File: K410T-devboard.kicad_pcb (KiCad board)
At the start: 2 copper layers, 120 x 120 mm, 30 parts, among them U1 XC7K410T-2FFG900I

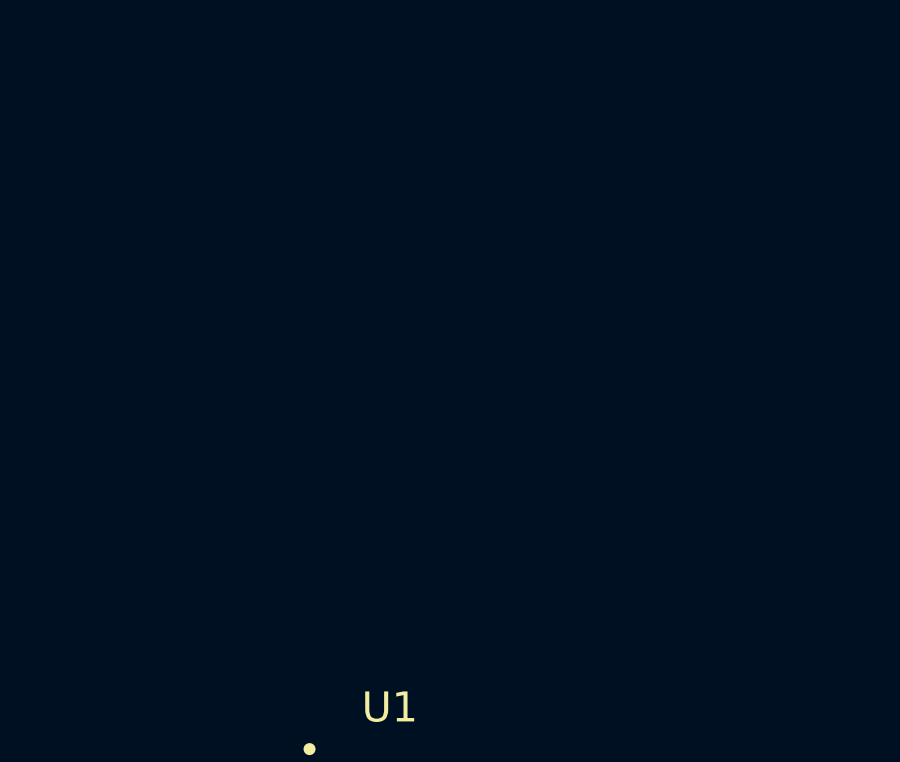
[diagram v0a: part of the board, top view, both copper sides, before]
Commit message: Add MT41K512M8DA DDR3L
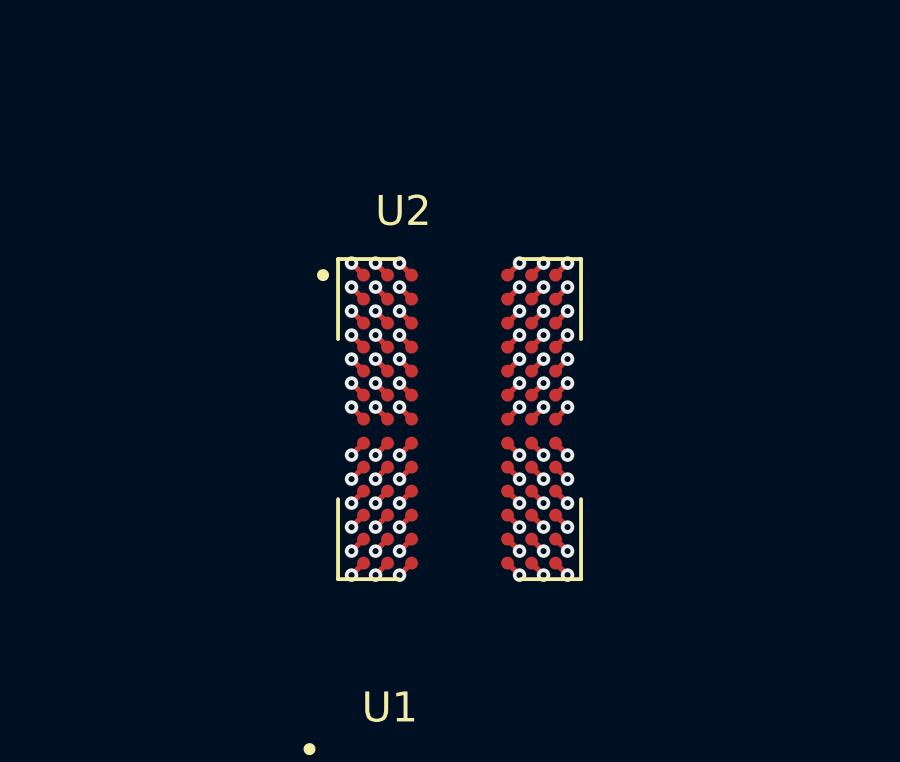
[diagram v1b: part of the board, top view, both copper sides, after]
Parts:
- added U2: MT41K512M8DA, antmicro-footprints:Micron_FBGA-78, F.Cu at (199.0, 103.0)
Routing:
- net VSS: track 0.00 -> 6.79 mm, vias 0 -> 12
- net VDD: track 0.00 -> 5.09 mm, vias 0 -> 9
- net (no net): track 0.00 -> 2.83 mm, vias 0 -> 5
- net VSSQ: track 0.00 -> 2.83 mm, vias 0 -> 5
- net VDDQ: track 0.00 -> 2.26 mm, vias 0 -> 4
- net unconnected-(U2-PadN8): track 0.00 -> 0.57 mm, vias 0 -> 1
- net unconnected-(U2-PadN7): track 0.00 -> 0.57 mm, vias 0 -> 1
- net unconnected-(U2-PadN3): track 0.00 -> 0.57 mm, vias 0 -> 1
- net unconnected-(U2-PadN2): track 0.00 -> 0.57 mm, vias 0 -> 1
- net unconnected-(U2-PadM8): track 0.00 -> 0.57 mm, vias 0 -> 1
- net unconnected-(U2-PadM7): track 0.00 -> 0.57 mm, vias 0 -> 1
- net unconnected-(U2-PadM3): track 0.00 -> 0.57 mm, vias 0 -> 1
- net unconnected-(U2-PadM2): track 0.00 -> 0.57 mm, vias 0 -> 1
- net unconnected-(U2-PadJ8): track 0.00 -> 0.57 mm, vias 0 -> 1
- net unconnected-(U2-PadJ7): track 0.00 -> 0.57 mm, vias 0 -> 1
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
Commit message: Update project files naming, reorganize hierarchical sheet structure, power supply WIP
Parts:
- added C30: C_100n_0201, antmicro-footprints:0201-res, F.Cu at (153.9, 63.9)
- added C31: C_100n_0201, antmicro-footprints:0201-res, F.Cu at (153.9, 62.1)
- added C32: C_100n_0201, antmicro-footprints:0201-res, F.Cu at (154.5, 56.4)
- added C33: C_100n_0201, antmicro-footprints:0201-res, F.Cu at (182.0, 38.1)
- added C34: C_100n_0201, antmicro-footprints:0201-res, F.Cu at (180.9, 39.9)
- added C35: C_100n_0201, antmicro-footprints:0201-res, F.Cu at (177.1, 36.4)
- added C36: C_10u_0402, antmicro-footprints:0402-cap, F.Cu at (169.0, 38.5)
- added C37: C_100n_0201, antmicro-footprints:0201-res, F.Cu at (165.2, 46.3)
- added C38: C_100n_0201, antmicro-footprints:0201-res, F.Cu at (165.2, 51.6)
- added C39: C_100n_0201, antmicro-footprints:0201-res, F.Cu at (174.6, 36.4)
- added C40: C_100n_0201, antmicro-footprints:0201-res, F.Cu at (170.1, 49.1)
- added C41: C_100n_0201, antmicro-footprints:0201-res, F.Cu at (170.6, 45.6)
- added C42: C_10u_0402, antmicro-footprints:0402-cap, F.Cu at (171.9, 36.5)
- added C43: C_10u_0402, antmicro-footprints:0402-cap, F.Cu at (165.5, 44.5)
- added C44: C_100n_0201, antmicro-footprints:0201-res, F.Cu at (182.0, 36.4)
- added C45: C_100n_0201, antmicro-footprints:0201-res, F.Cu at (172.6, 47.4)
- added C46: C_100n_0201, antmicro-footprints:0201-res, F.Cu at (173.1, 43.9)
- added C47: C_100n_0201, antmicro-footprints:0201-res, F.Cu at (167.7, 47.0)
- added C48: C_100n_0201, antmicro-footprints:0201-res, F.Cu at (177.1, 38.1)
- added C49: C_100n_0201, antmicro-footprints:0201-res, F.Cu at (167.7, 48.7)
- added C50: C_4u7_0402, antmicro-footprints:0402-cap, F.Cu at (168.4, 40.5)
- added C51: C_4u7_0402, antmicro-footprints:0402-cap, F.Cu at (165.5, 40.5)
- added C52: C_47u_0603, antmicro-footprints:0603-cap, F.Cu at (165.8, 36.8)
- added C53: C_47u_0603, antmicro-footprints:0603-cap, F.Cu at (151.5, 56.7)
- added C54: C_10u_25V_0603, antmicro-footprints:0603-cap, F.Cu at (200.6, 47.2)
- added C55: C_10u_25V_0603, antmicro-footprints:0603-cap, F.Cu at (204.4, 43.6)
- added C56: C_10u_25V_0603, antmicro-footprints:0603-cap, F.Cu at (204.1, 48.6)
- added C57: C_10u_25V_0603, antmicro-footprints:0603-cap, F.Cu at (207.9, 43.6)
- added C58: C_100n_0402, antmicro-footprints:0402-cap, F.Cu at (213.6, 36.5)
- added C59: C_100n_0402, antmicro-footprints:0402-cap, F.Cu at (211.2, 43.4)
- added C60: C_47u_0603, antmicro-footprints:0603-cap, F.Cu at (200.6, 49.7)
- added C61: C_47u_0603, antmicro-footprints:0603-cap, F.Cu at (207.9, 46.1)
- added C62: C_47u_0603, antmicro-footprints:0603-cap, F.Cu at (200.6, 52.2)
- added C63: C_47u_0603, antmicro-footprints:0603-cap, F.Cu at (204.4, 46.1)
- added L1: XAL5030-122MEC, antmicro-footprints:Coilcraft-XAL5030, F.Cu at (208.8, 39.0)
- added L2: XAL5030-122MEC, antmicro-footprints:Coilcraft-XAL5030, F.Cu at (202.2, 39.0)
- added Q1: SIA906EDJ-T1-GE3, antmicro-footprints:VISHAY_PowerPAK_SC70-6L, F.Cu at (200.8, 44.2)
- added R1: R_80R6_0402, antmicro-footprints:0402-res, F.Cu at (151.2, 62.3)
- added R10: R_40R2_0201, antmicro-footprints:0201-res, F.Cu at (173.5, 40.1)
- added R11: R_40R2_0201, antmicro-footprints:0201-res, F.Cu at (184.4, 36.4)
- added R12: R_40R2_0201, antmicro-footprints:0201-res, F.Cu at (173.5, 41.9)
- added R13: R_40R2_0201, antmicro-footprints:0201-res, F.Cu at (165.2, 49.8)
- added R14: R_40R2_0201, antmicro-footprints:0201-res, F.Cu at (167.7, 50.5)
- added R15: R_40R2_0201, antmicro-footprints:0201-res, F.Cu at (159.4, 56.4)
- added R16: R_40R2_0201, antmicro-footprints:0201-res, F.Cu at (179.5, 38.1)
- added R17: R_40R2_0201, antmicro-footprints:0201-res, F.Cu at (176.0, 41.6)
- added R18: R_40R2_0201, antmicro-footprints:0201-res, F.Cu at (176.0, 39.9)
- added R19: R_40R2_0201, antmicro-footprints:0201-res, F.Cu at (178.4, 39.9)
- added R2: R_80R6_0402, antmicro-footprints:0402-res, F.Cu at (151.2, 64.3)
- added R20: R_40R2_0201, antmicro-footprints:0201-res, F.Cu at (164.3, 56.4)
- added R21: R_40R2_0201, antmicro-footprints:0201-res, F.Cu at (165.2, 48.1)
- added R22: R_40R2_0201, antmicro-footprints:0201-res, F.Cu at (161.9, 56.4)
- added R23: R_100R_0201, antmicro-footprints:0201-res, F.Cu at (173.1, 45.6)
- added R24: R_40R2_0201, antmicro-footprints:0201-res, F.Cu at (171.1, 42.1)
- added R25: R_10k_0402, antmicro-footprints:0402-res, F.Cu at (165.5, 42.5)
- added R26: R_240R_1%_0402, antmicro-footprints:0402-res, F.Cu at (169.0, 36.5)
- added R27: 4x39R_0201_array, antmicro-footprints:EXB18V, F.Cu at (168.1, 42.9)
- added R28: R_40R2_0201, antmicro-footprints:0201-res, F.Cu at (178.4, 41.6)
- added R29: R_40R2_0201, antmicro-footprints:0201-res, F.Cu at (170.6, 43.9)
- added R3: R_40R2_0201, antmicro-footprints:0201-res, F.Cu at (179.5, 36.4)
- added R30: R_40R2_0201, antmicro-footprints:0201-res, F.Cu at (157.0, 56.4)
- added R31: R_40R2_0201, antmicro-footprints:0201-res, F.Cu at (175.5, 43.6)
- added R32: R_40R2_0201, antmicro-footprints:0201-res, F.Cu at (171.1, 40.4)
- added R33: R_22k_0402, antmicro-footprints:0402-res, F.Cu at (213.6, 38.5)
- added R34: R_22k_0402, antmicro-footprints:0402-res, F.Cu at (213.6, 40.5)
- added R4: R_40R2_0201, antmicro-footprints:0201-res, F.Cu at (174.6, 38.1)
- added R5: R_40R2_0201, antmicro-footprints:0201-res, F.Cu at (168.2, 45.2)
- added R6: R_40R2_0201, antmicro-footprints:0201-res, F.Cu at (170.1, 47.4)
- added R7: R_40R2_0201, antmicro-footprints:0201-res, F.Cu at (167.7, 52.2)
- added R8: R_40R2_0201, antmicro-footprints:0201-res, F.Cu at (165.2, 53.3)
- added R9: R_40R2_0201, antmicro-footprints:0201-res, F.Cu at (171.7, 38.4)
- added U3: ADP5054ACPZ-R7, antmicro-footprints:Analog_CP_48_13, F.Cu at (194.2, 49.6)
- added U4: ADP5050ACPZ-R7, antmicro-footprints:Analog_CP_48_13, F.Cu at (194.2, 40.2)
- added U5: AS6C8008-55ZIN, antmicro-footprints:TSOP-II-44_10.16x18.41mm_P0.8mm, F.Cu at (156.9, 45.5)
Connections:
- U1 pad AB7: unconnected-(U1-PadAB7) -> Net-(R2-Pad1)
- U1 pad AC1: unconnected-(U1-PadAC1) -> /FPGA banks 33-34/DDR.A12
- U1 pad AC2: unconnected-(U1-PadAC2) -> /FPGA banks 33-34/DDR.A13
- U1 pad AC4: unconnected-(U1-PadAC4) -> /FPGA banks 33-34/DDR.A10
- U1 pad AC5: unconnected-(U1-PadAC5) -> /FPGA banks 33-34/DDR.A11
- U1 pad AC6: unconnected-(U1-PadAC6) -> /FPGA banks 33-34/DDR_VRN
- U1 pad AC7: unconnected-(U1-PadAC7) -> /FPGA banks 33-34/DDR.A7
- U1 pad AD1: unconnected-(U1-PadAD1) -> /FPGA banks 33-34/DDR.CK_N
- U1 pad AD2: unconnected-(U1-PadAD2) -> /FPGA banks 33-34/DDR.CK_P
- U1 pad AD3: unconnected-(U1-PadAD3) -> /FPGA banks 33-34/DDR.A14
- U1 pad AD4: unconnected-(U1-PadAD4) -> /FPGA banks 33-34/DDR.A15
- U1 pad AD6: unconnected-(U1-PadAD6) -> /FPGA banks 33-34/DDR.A9
- U1 pad AD7: unconnected-(U1-PadAD7) -> /FPGA banks 33-34/+0.676_VTT
- U1 pad AE1: unconnected-(U1-PadAE1) -> /FPGA banks 33-34/DDR.A4
- U1 pad AE3: unconnected-(U1-PadAE3) -> /FPGA banks 33-34/DDR.BA2
- U1 pad AE4: unconnected-(U1-PadAE4) -> /FPGA banks 33-34/DDR.A0
- U1 pad AE5: unconnected-(U1-PadAE5) -> /FPGA banks 33-34/DDR.BA1
- U1 pad AE6: unconnected-(U1-PadAE6) -> /FPGA banks 33-34/DDR.A8
- U1 pad AF1: unconnected-(U1-PadAF1) -> /FPGA banks 33-34/DDR.A3
- U1 pad AF2: unconnected-(U1-PadAF2) -> /FPGA banks 33-34/DDR.A5
- U1 pad AF3: unconnected-(U1-PadAF3) -> /FPGA banks 33-34/DDR.A6
- U1 pad AF5: unconnected-(U1-PadAF5) -> /FPGA banks 33-34/DDR.BA0
- U1 pad AF6: unconnected-(U1-PadAF6) -> /FPGA banks 33-34/DDR.~{CAS}
- U1 pad AF7: unconnected-(U1-PadAF7) -> /FPGA banks 33-34/DDR.DQ0
- U1 pad AF8: unconnected-(U1-PadAF8) -> /FPGA banks 33-34/DDR.DM
- U1 pad AG2: unconnected-(U1-PadAG2) -> /FPGA banks 33-34/DDR.~{WE}
- U1 pad AG3: unconnected-(U1-PadAG3) -> /FPGA banks 33-34/DDR.A1
- U1 pad AG4: unconnected-(U1-PadAG4) -> /FPGA banks 33-34/DDR.A2
- U1 pad AG5: unconnected-(U1-PadAG5) -> /FPGA banks 33-34/DDR.~{RAS}
- U1 pad AG7: unconnected-(U1-PadAG7) -> /FPGA banks 33-34/DDR.DQ1
- U1 pad AG8: unconnected-(U1-PadAG8) -> /FPGA banks 33-34/+0.676_VTT
- U1 pad AH1: unconnected-(U1-PadAH1) -> /FPGA banks 33-34/DDR.~{CS}
- U1 pad AH2: unconnected-(U1-PadAH2) -> /FPGA banks 33-34/DDR.CKE
- U1 pad AH4: unconnected-(U1-PadAH4) -> /FPGA banks 33-34/DDR.~{RESET}
- U1 pad AH7: unconnected-(U1-PadAH7) -> /FPGA banks 33-34/DDR.DQS_P
- U1 pad AJ2: unconnected-(U1-PadAJ2) -> /FPGA banks 33-34/DDR.ODT
- U1 pad AJ6: unconnected-(U1-PadAJ6) -> /FPGA banks 33-34/DDR.DQ2
- U1 pad AJ7: unconnected-(U1-PadAJ7) -> /FPGA banks 33-34/DDR.DQS_N
- U1 pad AJ8: unconnected-(U1-PadAJ8) -> /FPGA banks 33-34/DDR.DQ4
- U1 pad AK4: unconnected-(U1-PadAK4) -> /FPGA banks 33-34/DDR.DQ7
- U1 pad AK5: unconnected-(U1-PadAK5) -> /FPGA banks 33-34/DDR.DQ6
- U1 pad AK6: unconnected-(U1-PadAK6) -> /FPGA banks 33-34/DDR.DQ3
- U1 pad AK8: unconnected-(U1-PadAK8) -> /FPGA banks 33-34/DDR.DQ5
- U1 pad P26: unconnected-(U1-PadP26) -> /FPGA banks 12-15/SRAM.~{OE}
- U1 pad P27: unconnected-(U1-PadP27) -> /FPGA banks 12-15/SRAM.A5
- U1 pad P28: unconnected-(U1-PadP28) -> /FPGA banks 12-15/SRAM.A6
- U1 pad P29: unconnected-(U1-PadP29) -> /FPGA banks 12-15/SRAM.DQ3
- U1 pad R26: unconnected-(U1-PadR26) -> /FPGA banks 12-15/SRAM.A8
- U1 pad R28: unconnected-(U1-PadR28) -> /FPGA banks 12-15/SRAM.DQ6
- U1 pad R29: unconnected-(U1-PadR29) -> /FPGA banks 12-15/SRAM.DQ7
- U1 pad R30: unconnected-(U1-PadR30) -> /FPGA banks 12-15/SRAM.A9
- U1 pad T25: unconnected-(U1-PadT25) -> /FPGA banks 12-15/SRAM.A2
- U1 pad T26: unconnected-(U1-PadT26) -> /FPGA banks 12-15/SRAM.A3
- U1 pad T27: unconnected-(U1-PadT27) -> /FPGA banks 12-15/SRAM.A13
- U1 pad T28: unconnected-(U1-PadT28) -> /FPGA banks 12-15/SRAM.DQ5
- U1 pad T30: unconnected-(U1-PadT30) -> /FPGA banks 12-15/SRAM.A15
- U1 pad U20: unconnected-(U1-PadU20) -> /FPGA banks 12-15/SRAM.DQ4
- U1 pad U22: unconnected-(U1-PadU22) -> /FPGA banks 12-15/SRAM.CE2
- U1 pad U23: unconnected-(U1-PadU23) -> /FPGA banks 12-15/SRAM.A14
- U1 pad U25: unconnected-(U1-PadU25) -> /FPGA banks 12-15/SRAM.A11
- U1 pad U27: unconnected-(U1-PadU27) -> /FPGA banks 12-15/SRAM.A10
- U1 pad U28: unconnected-(U1-PadU28) -> /FPGA banks 12-15/SRAM.A0
- U1 pad V19: unconnected-(U1-PadV19) -> /FPGA banks 12-15/SRAM.A12
- U1 pad V20: unconnected-(U1-PadV20) -> /FPGA banks 12-15/SRAM.A4
- U1 pad V21: unconnected-(U1-PadV21) -> /FPGA banks 12-15/SRAM.DQ0
- U1 pad V24: unconnected-(U1-PadV24) -> /FPGA banks 12-15/SRAM.A7
- U1 pad V25: unconnected-(U1-PadV25) -> /FPGA banks 12-15/SRAM.A18
- U1 pad V27: unconnected-(U1-PadV27) -> /FPGA banks 12-15/SRAM.~{CE}
- U1 pad V29: unconnected-(U1-PadV29) -> /FPGA banks 12-15/SRAM.A1
- U1 pad V30: unconnected-(U1-PadV30) -> /FPGA banks 12-15/SRAM.DQ1
- U1 pad W21: unconnected-(U1-PadW21) -> /FPGA banks 12-15/SRAM.DQ2
- U1 pad W22: unconnected-(U1-PadW22) -> /FPGA banks 12-15/SRAM.~{WE}
- U1 pad W23: unconnected-(U1-PadW23) -> /FPGA banks 12-15/SRAM.A16
- U1 pad W24: unconnected-(U1-PadW24) -> /FPGA banks 12-15/SRAM.A17
- U1 pad W26: unconnected-(U1-PadW26) -> /FPGA banks 12-15/SRAM.A19
- U2 pad A1: VSS -> GND
- U2 pad A2: VDD -> +1V35
- U2 pad A8: VSS -> GND
- U2 pad A9: VDD -> +1V35
- U2 pad B1: VSS -> GND
- U2 pad B2: VSSQ -> GND
- U2 pad B3: unconnected-(U2-PadB3) -> /FPGA banks 33-34/DDR.DQ0
- U2 pad B7: unconnected-(U2-PadB7) -> /FPGA banks 33-34/DDR.DM
- U2 pad B8: VSSQ -> GND
- U2 pad B9: VDDQ -> +1V35
- U2 pad C1: VDDQ -> +1V35
- U2 pad C2: unconnected-(U2-PadC2) -> /FPGA banks 33-34/DDR.DQ2
- U2 pad C3: unconnected-(U2-PadC3) -> /FPGA banks 33-34/DDR.DQS_P
- U2 pad C7: unconnected-(U2-PadC7) -> /FPGA banks 33-34/DDR.DQ1
- U2 pad C8: unconnected-(U2-PadC8) -> /FPGA banks 33-34/DDR.DQ3
- U2 pad C9: VSSQ -> GND
- U2 pad D1: VSSQ -> GND
- U2 pad D2: unconnected-(U2-PadD2) -> /FPGA banks 33-34/DDR.DQ6
- U2 pad D3: unconnected-(U2-PadD3) -> /FPGA banks 33-34/DDR.DQS_N
- U2 pad D7: VDD -> +1V35
- U2 pad D8: VSS -> GND
- U2 pad D9: VSSQ -> GND
- U2 pad E1: unconnected-(U2-PadE1) -> /RAM/+0.676_VREF
- U2 pad E2: VDDQ -> +1V35
- U2 pad E3: unconnected-(U2-PadE3) -> /FPGA banks 33-34/DDR.DQ4
- U2 pad E7: unconnected-(U2-PadE7) -> /FPGA banks 33-34/DDR.DQ7
- U2 pad E8: unconnected-(U2-PadE8) -> /FPGA banks 33-34/DDR.DQ5
- U2 pad E9: VDDQ -> +1V35
- U2 pad F2: VSS -> GND
- U2 pad F3: unconnected-(U2-PadF3) -> /FPGA banks 33-34/DDR.~{RAS}
- U2 pad F7: unconnected-(U2-PadF7) -> /FPGA banks 33-34/DDR.CK_P
- U2 pad F8: VSS -> GND
- U2 pad G1: unconnected-(U2-PadG1) -> /FPGA banks 33-34/DDR.ODT
- U2 pad G2: VDD -> +1V35
- U2 pad G3: unconnected-(U2-PadG3) -> /FPGA banks 33-34/DDR.~{CAS}
- U2 pad G7: unconnected-(U2-PadG7) -> /FPGA banks 33-34/DDR.CK_N
- U2 pad G8: VDD -> +1V35
- U2 pad G9: unconnected-(U2-PadG9) -> /FPGA banks 33-34/DDR.CKE
- U2 pad H2: unconnected-(U2-PadH2) -> /FPGA banks 33-34/DDR.~{CS}
- U2 pad H3: unconnected-(U2-PadH3) -> /FPGA banks 33-34/DDR.~{WE}
- U2 pad H7: unconnected-(U2-PadH7) -> /FPGA banks 33-34/DDR.A10
- U2 pad H8: unconnected-(U2-PadH8) -> /RAM/DDR_ZQ
- U2 pad J1: VSS -> GND
- U2 pad J2: unconnected-(U2-PadJ2) -> /FPGA banks 33-34/DDR.BA0
- U2 pad J3: unconnected-(U2-PadJ3) -> /FPGA banks 33-34/DDR.BA2
- U2 pad J7: unconnected-(U2-PadJ7) -> /FPGA banks 33-34/DDR.A15
- U2 pad J8: unconnected-(U2-PadJ8) -> /RAM/+0.676_VREF
- U2 pad J9: VSS -> GND
- U2 pad K1: VDD -> +1V35
- U2 pad K2: unconnected-(U2-PadK2) -> /FPGA banks 33-34/DDR.A3
- U2 pad K3: unconnected-(U2-PadK3) -> /FPGA banks 33-34/DDR.A0
- U2 pad K7: unconnected-(U2-PadK7) -> /FPGA banks 33-34/DDR.A12
- U2 pad K8: unconnected-(U2-PadK8) -> /FPGA banks 33-34/DDR.BA1
- U2 pad K9: VDD -> +1V35
- U2 pad L1: VSS -> GND
- U2 pad L2: unconnected-(U2-PadL2) -> /FPGA banks 33-34/DDR.A5
- U2 pad L3: unconnected-(U2-PadL3) -> /FPGA banks 33-34/DDR.A2
- U2 pad L7: unconnected-(U2-PadL7) -> /FPGA banks 33-34/DDR.A1
- U2 pad L8: unconnected-(U2-PadL8) -> /FPGA banks 33-34/DDR.A4
- U2 pad L9: VSS -> GND
- U2 pad M1: VDD -> +1V35
- U2 pad M2: unconnected-(U2-PadM2) -> /FPGA banks 33-34/DDR.A7
- U2 pad M3: unconnected-(U2-PadM3) -> /FPGA banks 33-34/DDR.A9
- U2 pad M7: unconnected-(U2-PadM7) -> /FPGA banks 33-34/DDR.A11
- U2 pad M8: unconnected-(U2-PadM8) -> /FPGA banks 33-34/DDR.A6
- U2 pad M9: VDD -> +1V35
- U2 pad N1: VSS -> GND
- U2 pad N2: unconnected-(U2-PadN2) -> /FPGA banks 33-34/DDR.~{RESET}
- U2 pad N3: unconnected-(U2-PadN3) -> /FPGA banks 33-34/DDR.A13
- U2 pad N7: unconnected-(U2-PadN7) -> /FPGA banks 33-34/DDR.A14
- U2 pad N8: unconnected-(U2-PadN8) -> /FPGA banks 33-34/DDR.A8
- U2 pad N9: VSS -> GND
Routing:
- net GND: track 122.3 -> 131.9 mm, vias 173 -> 190
- net +1V35: track 0.00 -> 7.35 mm, vias 0 -> 13
- net VSS: track 6.79 -> 0.00 mm, vias 12 -> 0
- net VDD: track 5.09 -> 0.00 mm, vias 9 -> 0
- net VSSQ: track 2.83 -> 0.00 mm, vias 5 -> 0
- net VDDQ: track 2.26 -> 0.00 mm, vias 4 -> 0
- net /FPGA banks 33-34/+0.676_VTT: track 0.00 -> 1.41 mm, vias 0 -> 2
- net /FPGA banks 33-34/DDR.~{WE}: track 0.00 -> 1.27 mm, vias 0 -> 2
- net /FPGA banks 33-34/DDR.~{RESET}: track 0.00 -> 1.27 mm, vias 0 -> 2
- net /FPGA banks 33-34/DDR.~{RAS}: track 0.00 -> 1.27 mm, vias 0 -> 2
- net /FPGA banks 33-34/DDR.~{CS}: track 0.00 -> 1.27 mm, vias 0 -> 2
- net /FPGA banks 33-34/DDR.~{CAS}: track 0.00 -> 1.27 mm, vias 0 -> 2
- net /FPGA banks 33-34/DDR.ODT: track 0.00 -> 1.27 mm, vias 0 -> 2
- net /FPGA banks 33-34/DDR.DQ7: track 0.00 -> 1.27 mm, vias 0 -> 2
- net /FPGA banks 33-34/DDR.DQ5: track 0.00 -> 1.27 mm, vias 0 -> 2
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
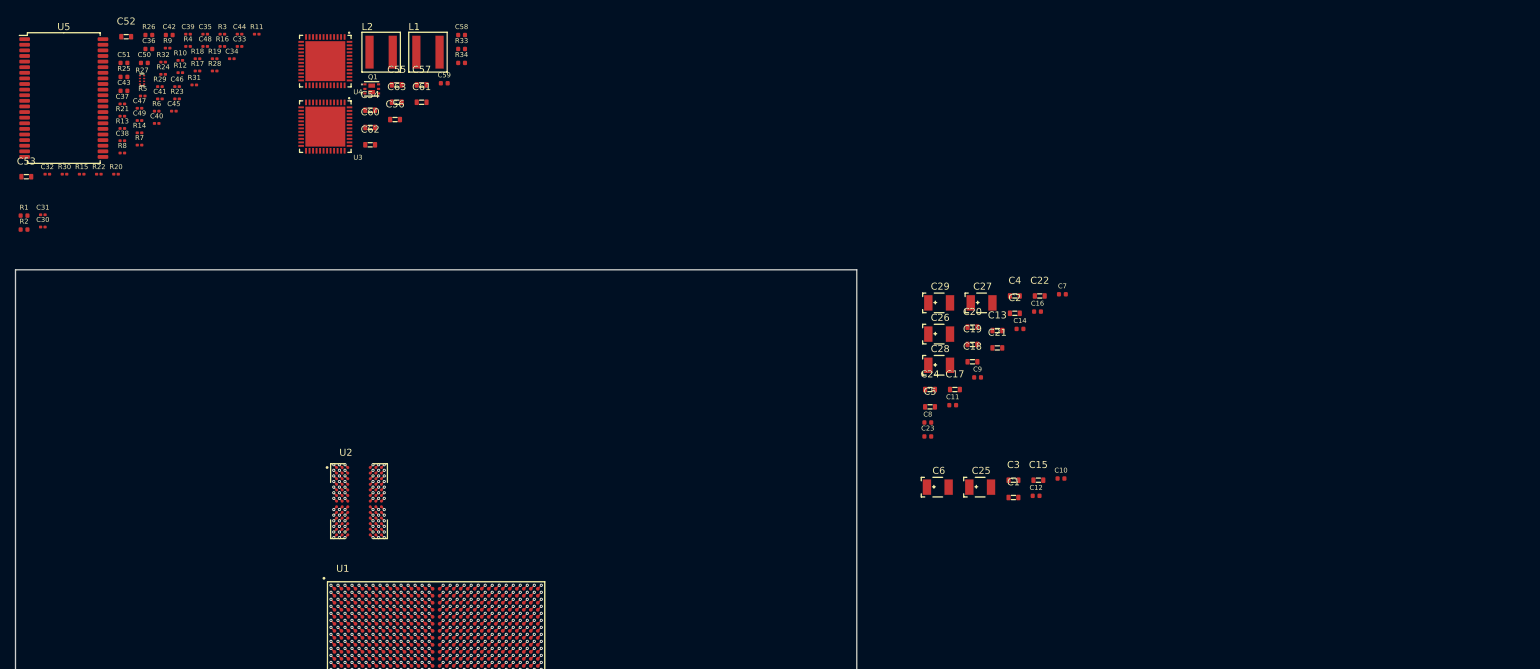
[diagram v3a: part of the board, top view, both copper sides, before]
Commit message: Add FPGA planar decoupling, finish DC-DC for 1V2, 1V35, 1V8, 3V3 and MGTAVCC rails
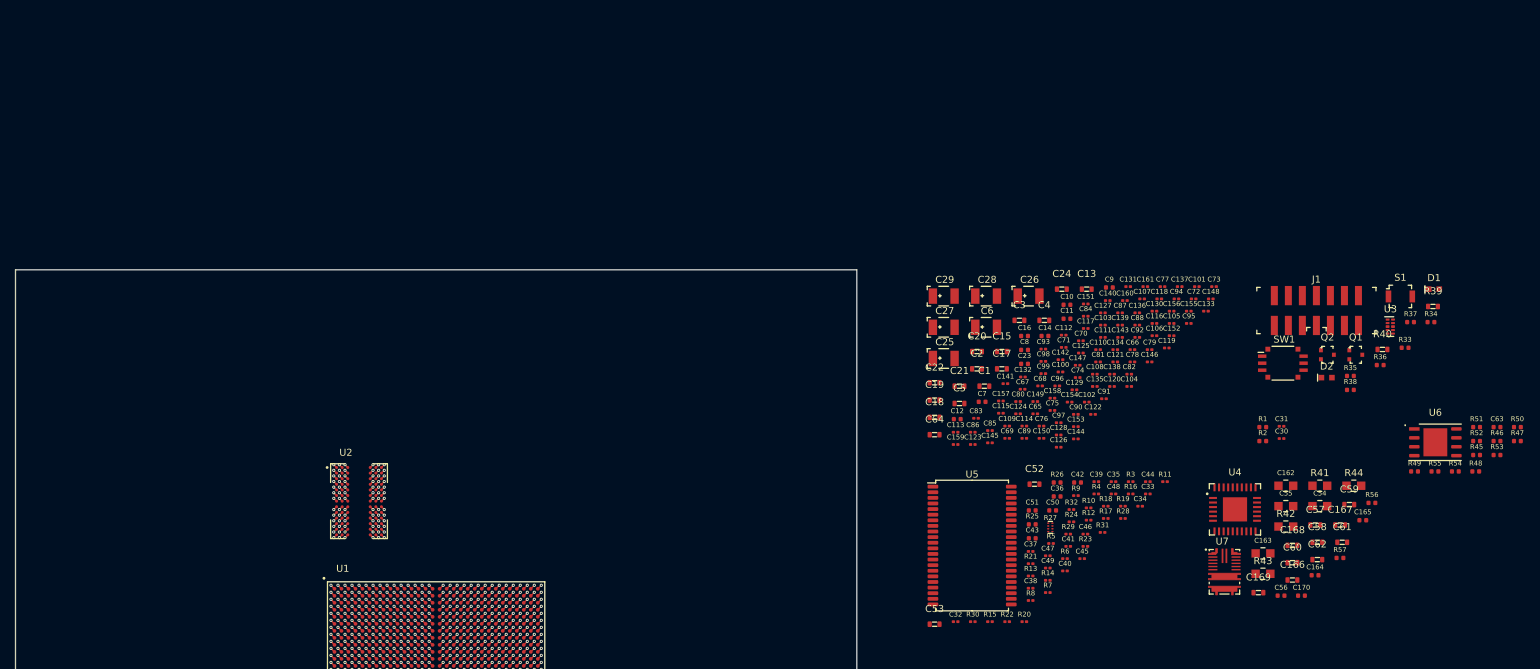
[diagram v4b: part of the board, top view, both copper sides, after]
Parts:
- removed L1, L2: XAL5030-122MEC, antmicro-footprints:Coilcraft-XAL5030
- added C100: C_100n_0201, antmicro-footprints:0201-res, F.Cu at (299.1, 84.6)
- added C101: C_100n_0201, antmicro-footprints:0201-res, F.Cu at (318.5, 72.4)
- added C102: C_100n_0201, antmicro-footprints:0201-res, F.Cu at (302.8, 88.9)
- added C103: C_100n_0201, antmicro-footprints:0201-res, F.Cu at (305.1, 77.9)
- added C104: C_100n_0201, antmicro-footprints:0201-res, F.Cu at (308.9, 86.6)
- added C105: C_100n_0201, antmicro-footprints:0201-res, F.Cu at (314.9, 77.7)
- added C106: C_100n_0201, antmicro-footprints:0201-res, F.Cu at (312.5, 79.4)
- added C107: C_100n_0201, antmicro-footprints:0201-res, F.Cu at (310.7, 74.2)
- added C108: C_100n_0201, antmicro-footprints:0201-res, F.Cu at (304.0, 84.9)
- added C109: C_100n_0201, antmicro-footprints:0201-res, F.Cu at (291.4, 92.3)
- added C110: C_100n_0201, antmicro-footprints:0201-res, F.Cu at (304.4, 81.4)
- added C111: C_100n_0201, antmicro-footprints:0201-res, F.Cu at (305.1, 79.6)
- added C112: C_100n_0201, antmicro-footprints:0201-res, F.Cu at (299.5, 79.3)
- added C113: C_100n_0201, antmicro-footprints:0201-res, F.Cu at (284.1, 93.2)
- added C114: C_100n_0201, antmicro-footprints:0201-res, F.Cu at (293.9, 92.3)
- added C115: C_100n_0201, antmicro-footprints:0201-res, F.Cu at (290.6, 90.5)
- added C116: C_100n_0201, antmicro-footprints:0201-res, F.Cu at (312.5, 77.7)
- added C117: C_100n_0201, antmicro-footprints:0201-res, F.Cu at (302.7, 78.4)
- added C118: C_100n_0201, antmicro-footprints:0201-res, F.Cu at (313.1, 74.2)
- added C119: C_100n_0201, antmicro-footprints:0201-res, F.Cu at (314.2, 81.2)
- added C120: C_100n_0201, antmicro-footprints:0201-res, F.Cu at (306.4, 86.6)
- added C121: C_100n_0201, antmicro-footprints:0201-res, F.Cu at (306.9, 83.1)
- added C122: C_100n_0201, antmicro-footprints:0201-res, F.Cu at (303.7, 90.6)
- added C123: C_100n_0201, antmicro-footprints:0201-res, F.Cu at (286.6, 94.9)
- added C124: C_100n_0201, antmicro-footprints:0201-res, F.Cu at (293.0, 90.5)
- added C125: C_100n_0201, antmicro-footprints:0201-res, F.Cu at (302.0, 81.9)
- added C126: C_100n_0201, antmicro-footprints:0201-res, F.Cu at (298.8, 95.3)
- added C127: C_100n_0201, antmicro-footprints:0201-res, F.Cu at (305.1, 76.1)
- added C128: C_100n_0201, antmicro-footprints:0201-res, F.Cu at (298.8, 93.6)
- added C129: C_100n_0201, antmicro-footprints:0201-res, F.Cu at (301.1, 87.1)
- added C130: C_100n_0201, antmicro-footprints:0201-res, F.Cu at (312.5, 75.9)
- added C131: C_100n_0201, antmicro-footprints:0201-res, F.Cu at (308.7, 72.4)
- added C132: C_100n_0201, antmicro-footprints:0201-res, F.Cu at (293.7, 85.3)
- added C133: C_100n_0201, antmicro-footprints:0201-res, F.Cu at (319.8, 75.9)
- added C134: C_100n_0201, antmicro-footprints:0201-res, F.Cu at (306.9, 81.4)
- added C135: C_100n_0201, antmicro-footprints:0201-res, F.Cu at (304.0, 86.6)
- added C136: C_100n_0201, antmicro-footprints:0201-res, F.Cu at (310.0, 76.1)
- added C137: C_100n_0201, antmicro-footprints:0201-res, F.Cu at (316.1, 72.4)
- added C138: C_100n_0201, antmicro-footprints:0201-res, F.Cu at (306.4, 84.9)
- added C139: C_100n_0201, antmicro-footprints:0201-res, F.Cu at (307.6, 77.9)
- added C140: C_100n_0201, antmicro-footprints:0201-res, F.Cu at (305.8, 74.4)
- added C141: C_100n_0201, antmicro-footprints:0201-res, F.Cu at (291.2, 86.2)
- added C142: C_100n_0201, antmicro-footprints:0201-res, F.Cu at (299.1, 82.8)
- added C143: C_100n_0201, antmicro-footprints:0201-res, F.Cu at (307.6, 79.6)
- added C144: C_100n_0201, antmicro-footprints:0201-res, F.Cu at (301.2, 94.1)
- added C145: C_100n_0201, antmicro-footprints:0201-res, F.Cu at (289.0, 94.7)
- added C146: C_100n_0201, antmicro-footprints:0201-res, F.Cu at (311.8, 83.1)
- added C147: C_100n_0201, antmicro-footprints:0201-res, F.Cu at (301.5, 83.6)
- added C148: C_100n_0201, antmicro-footprints:0201-res, F.Cu at (320.5, 74.2)
- added C149: C_100n_0201, antmicro-footprints:0201-res, F.Cu at (295.5, 88.8)
- added C150: C_100n_0201, antmicro-footprints:0201-res, F.Cu at (296.4, 94.0)
- added C151: C_100n_0201, antmicro-footprints:0201-res, F.Cu at (302.7, 74.9)
- added C152: C_100n_0201, antmicro-footprints:0201-res, F.Cu at (314.9, 79.4)
- added C153: C_100n_0201, antmicro-footprints:0201-res, F.Cu at (301.2, 92.4)
- added C154: C_100n_0201, antmicro-footprints:0201-res, F.Cu at (300.4, 88.9)
- added C155: C_100n_0201, antmicro-footprints:0201-res, F.Cu at (317.4, 75.9)
- added C156: C_100n_0201, antmicro-footprints:0201-res, F.Cu at (314.9, 75.9)
- added C157: C_100n_0201, antmicro-footprints:0201-res, F.Cu at (290.6, 88.7)
- added C158: C_100n_0201, antmicro-footprints:0201-res, F.Cu at (297.9, 88.3)
- added C159: C_100n_0201, antmicro-footprints:0201-res, F.Cu at (284.1, 94.9)
- added C160: C_100n_0201, antmicro-footprints:0201-res, F.Cu at (308.2, 74.4)
- added C161: C_100n_0201, antmicro-footprints:0201-res, F.Cu at (311.2, 72.4)
- added C162: C_22u_0805_25V, antmicro-footprints:0805-cap, F.Cu at (331.2, 100.8)
- added C163: C_22u_0805_25V, antmicro-footprints:0805-cap, F.Cu at (327.9, 110.5)
- added C164: C_100n_0402, antmicro-footprints:0402-cap, F.Cu at (335.4, 113.6)
- added C165: C_100n_0402, antmicro-footprints:0402-cap, F.Cu at (342.2, 105.7)
- added C166: C_22u_0603, antmicro-footprints:0603-cap, F.Cu at (332.1, 114.2)
- added C167: C_22u_0603, antmicro-footprints:0603-cap, F.Cu at (338.9, 106.4)
- added C168: C_22u_0603, antmicro-footprints:0603-cap, F.Cu at (332.1, 109.3)
- added C169: C_22u_0603, antmicro-footprints:0603-cap, F.Cu at (327.3, 116.0)
- added C170: C_39p_0402, antmicro-footprints:0402-cap, F.Cu at (333.4, 116.5)
- added C64: C_47u_0603, antmicro-footprints:0603-cap, F.Cu at (281.1, 93.5)
- added C65: C_100n_0201, antmicro-footprints:0201-res, F.Cu at (295.5, 90.5)
- added C66: C_100n_0201, antmicro-footprints:0201-res, F.Cu at (309.3, 81.4)
- added C67: C_100n_0201, antmicro-footprints:0201-res, F.Cu at (293.6, 87.0)
- added C68: C_100n_0201, antmicro-footprints:0201-res, F.Cu at (296.1, 86.6)
- added C69: C_100n_0201, antmicro-footprints:0201-res, F.Cu at (291.4, 94.0)
- added C70: C_100n_0201, antmicro-footprints:0201-res, F.Cu at (302.0, 80.1)
- added C71: C_100n_0201, antmicro-footprints:0201-res, F.Cu at (299.5, 81.1)
- added C72: C_100n_0201, antmicro-footprints:0201-res, F.Cu at (318.1, 74.2)
- added C73: C_100n_0201, antmicro-footprints:0201-res, F.Cu at (321.0, 72.4)
- added C74: C_100n_0201, antmicro-footprints:0201-res, F.Cu at (301.5, 85.4)
- added C75: C_100n_0201, antmicro-footprints:0201-res, F.Cu at (297.9, 90.1)
- added C76: C_100n_0201, antmicro-footprints:0201-res, F.Cu at (296.4, 92.3)
- added C77: C_100n_0201, antmicro-footprints:0201-res, F.Cu at (313.6, 72.4)
- added C78: C_100n_0201, antmicro-footprints:0201-res, F.Cu at (309.3, 83.1)
- added C79: C_100n_0201, antmicro-footprints:0201-res, F.Cu at (311.8, 81.4)
- added C80: C_100n_0201, antmicro-footprints:0201-res, F.Cu at (293.0, 88.8)
- added C81: C_100n_0201, antmicro-footprints:0201-res, F.Cu at (304.4, 83.1)
- added C82: C_100n_0201, antmicro-footprints:0201-res, F.Cu at (308.9, 84.9)
- added C83: C_100n_0201, antmicro-footprints:0201-res, F.Cu at (287.0, 91.2)
- added C84: C_100n_0201, antmicro-footprints:0201-res, F.Cu at (302.7, 76.6)
- added C85: C_100n_0201, antmicro-footprints:0201-res, F.Cu at (289.0, 92.9)
- added C86: C_100n_0201, antmicro-footprints:0201-res, F.Cu at (286.6, 93.2)
- added C87: C_100n_0201, antmicro-footprints:0201-res, F.Cu at (307.6, 76.1)
- added C88: C_100n_0201, antmicro-footprints:0201-res, F.Cu at (310.0, 77.9)
- added C89: C_100n_0201, antmicro-footprints:0201-res, F.Cu at (293.9, 94.0)
- added C90: C_100n_0201, antmicro-footprints:0201-res, F.Cu at (301.2, 90.6)
- added C91: C_100n_0201, antmicro-footprints:0201-res, F.Cu at (305.3, 88.4)
- added C92: C_100n_0201, antmicro-footprints:0201-res, F.Cu at (310.0, 79.6)
- added C93: C_100n_0201, antmicro-footprints:0201-res, F.Cu at (296.6, 81.3)
- added C94: C_100n_0201, antmicro-footprints:0201-res, F.Cu at (315.6, 74.2)
- added C95: C_100n_0201, antmicro-footprints:0201-res, F.Cu at (317.4, 77.7)
- added C96: C_100n_0201, antmicro-footprints:0201-res, F.Cu at (298.6, 86.6)
- added C97: C_100n_0201, antmicro-footprints:0201-res, F.Cu at (298.8, 91.8)
- added C98: C_100n_0201, antmicro-footprints:0201-res, F.Cu at (296.6, 83.1)
- added C99: C_100n_0201, antmicro-footprints:0201-res, F.Cu at (296.6, 84.8)
- added D1: KP-1608CGCK, antmicro-footprints:LED_0603, F.Cu at (352.3, 72.8)
- added D2: KP-1608CGCK, antmicro-footprints:LED_0603, F.Cu at (337.0, 85.4)
- added J1: 878321412, antmicro-footprints:PinHeader_2x7_P2mm_SMD_no_locator, F.Cu at (335.6, 75.8)
- added Q2: BSS138W-7-F, antmicro-footprints:SOT-323, F.Cu at (337.1, 82.1)
- added R35: R_10k_0402, antmicro-footprints:0402-res, F.Cu at (340.4, 85.1)
- added R36: R_10k_0402, antmicro-footprints:0402-res, F.Cu at (344.7, 83.6)
- added R37: R_10k_0402, antmicro-footprints:0402-res, F.Cu at (349.0, 77.5)
- added R38: R_10k_0402, antmicro-footprints:0402-res, F.Cu at (340.4, 87.1)
- added R39: R_330R_0603, antmicro-footprints:0603-res, F.Cu at (352.2, 75.2)
- added R40: R_330R_0603, antmicro-footprints:0603-res, F.Cu at (345.0, 81.4)
- added R41: R_0R_0805, antmicro-footprints:0805-res, F.Cu at (336.1, 100.8)
- added R42: R_0R_0805, antmicro-footprints:0805-res, F.Cu at (331.2, 106.6)
- added R43: R_0R_0805, antmicro-footprints:0805-res, F.Cu at (327.9, 113.4)
- added R44: R_0R_0805, antmicro-footprints:0805-res, F.Cu at (340.9, 100.8)
- added R45: R_10k_0402, antmicro-footprints:0402-res, F.Cu at (358.4, 96.4)
- added R46: R_10k_0402, antmicro-footprints:0402-res, F.Cu at (361.3, 94.4)
- added R47: R_10k_0402, antmicro-footprints:0402-res, F.Cu at (364.2, 94.4)
- added R48: R_100R_0402, antmicro-footprints:0402-res, F.Cu at (358.3, 98.8)
- added R49: R_100R_0402, antmicro-footprints:0402-res, F.Cu at (349.6, 98.8)
- added R50: R_0R_0402, antmicro-footprints:0402-res, F.Cu at (364.2, 92.4)
- added R51: R_0R_0402, antmicro-footprints:0402-res, F.Cu at (358.4, 92.4)
- added R52: R_0R_0402, antmicro-footprints:0402-res, F.Cu at (358.4, 94.4)
- added R53: R_0R_0402, antmicro-footprints:0402-res, F.Cu at (361.3, 96.4)
- added R54: R_0R_0402, antmicro-footprints:0402-res, F.Cu at (355.4, 98.8)
- added R55: R_0R_0402, antmicro-footprints:0402-res, F.Cu at (352.5, 98.8)
- added R56: R_20k_0402, antmicro-footprints:0402-res, F.Cu at (343.5, 103.2)
- added R57: R_4k42_0402, antmicro-footprints:0402-res, F.Cu at (338.9, 111.1)
- added S1: B3U-1000P, antmicro-footprints:Switch_Tactile_SMD_B3U-1000P, F.Cu at (347.5, 73.8)
- added SW1: CVS-03B, antmicro-footprints:SW_DIP_SPSTx03_Slide_Copal_CVS-03xB_W5.9mm_P1mm, F.Cu at (331.0, 83.3)
- added U6: MT25QL256ABA1EW7-0SIT, antmicro-footprints:WDFN-8-1EP_6x5mm_P1.27mm_EP3.4x4mm, F.Cu at (352.5, 94.6)
- added U7: MPM3650GQW-Z, antmicro-footprints:MPS_QFN24, F.Cu at (322.4, 113.1)
- C54, C55: value C_10u_25V_0603 -> C_22u_0805_25V; footprint antmicro-footprints:0603-cap -> antmicro-footprints:0805-cap
- C56: value C_10u_25V_0603 -> C_1u_0402; footprint antmicro-footprints:0603-cap -> antmicro-footprints:0402-cap
- C57: value C_10u_25V_0603 -> C_22u_0603
- C58, C59: value C_100n_0402 -> C_22u_0603; footprint antmicro-footprints:0402-cap -> antmicro-footprints:0603-cap
- C60, C61, C62: value C_47u_0603 -> C_22u_0603
- C63: value C_47u_0603 -> C_100n_0402; footprint antmicro-footprints:0603-cap -> antmicro-footprints:0402-cap
- Q1: value SIA906EDJ-T1-GE3 -> BSS138W-7-F; footprint antmicro-footprints:VISHAY_PowerPAK_SC70-6L -> antmicro-footprints:SOT-323
- R33, R34: value R_22k_0402 -> R_10k_0402
- U3: value ADP5054ACPZ-R7 -> TPD4E05U06QDQARQ1; footprint antmicro-footprints:Analog_CP_48_13 -> antmicro-footprints:USON-10_2.5x1.0mm_P0.5mm
- U4: value ADP5050ACPZ-R7 -> MPM54304GMN; footprint antmicro-footprints:Analog_CP_48_13 -> antmicro-footprints:MPS_LGA-33
- moved R1 179.2 mm to (327.9, 92.4)
- moved R2 179.2 mm to (327.9, 94.4)
- moved C30 179.2 mm to (330.6, 94.1)
- moved C31 179.2 mm to (330.6, 92.3)
- moved C63 163.6 mm to (361.3, 92.4)
- moved U3 154.6 mm to (346.1, 78.1)
- moved C62 147.5 mm to (335.7, 111.3)
- moved C54 146.8 mm to (336.1, 103.7)
- moved C61 145.5 mm to (339.2, 108.9)
- moved C60 145.5 mm to (332.1, 111.8)
- moved Q1 145.4 mm to (341.2, 82.1)
- moved U4 144.7 mm to (323.9, 104.2)
- moved C32 144.4 mm to (284.1, 120.2)
- moved C40 144.4 mm to (299.7, 113.0)
- moved C41 144.4 mm to (300.2, 109.5)
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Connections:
- C54 pad 2: GND -> Net-(C54-Pad2)
- C55 pad 2: GND -> Net-(C54-Pad2)
- C56 pad 1: VIN -> Net-(C56-Pad1)
- C57 pad 1: VIN -> VOUT1
- C58 pad 1: Net-(C58-Pad1) -> VOUT2
- C58 pad 2: Net-(C58-Pad2) -> GND
- C59 pad 1: Net-(C59-Pad1) -> VOUT1
- C59 pad 2: Net-(C59-Pad2) -> GND
- C60 pad 1: Net-(C60-Pad1) -> VOUT2
- C61 pad 1: GND -> Net-(C61-Pad1)
- C61 pad 2: Net-(C60-Pad1) -> GND
- C62 pad 1: Net-(C60-Pad1) -> VOUT4
- C63 pad 1: GND -> +3V3
- C63 pad 2: Net-(C60-Pad1) -> GND
- Q1 pad 1: GND -> /FPGA Config/DONE
- Q1 pad 2: Net-(Q1-Pad2) -> GND
- Q1 pad 3: Net-(C59-Pad1) -> Net-(Q1-Pad3)
- R33 pad 1: GND -> /FPGA Config/MODE2
- R33 pad 2: Net-(Q1-Pad2) -> +3V3
- R34 pad 1: Net-(Q1-Pad5) -> GND
- R34 pad 2: GND -> /FPGA Config/MODE1
- U1 pad A10: unconnected-(U1-PadA10) -> /FPGA Config/INIT_B
- U1 pad AB1: unconnected-(U1-PadAB1) -> /FPGA Config/MODE2
- U1 pad AB2: unconnected-(U1-PadAB2) -> /FPGA Config/MODE1
- U1 pad AB5: unconnected-(U1-PadAB5) -> /FPGA Config/MODE0
- U1 pad AB6: unconnected-(U1-PadAB6) -> VCCO_0
- U1 pad B10: unconnected-(U1-PadB10) -> /FPGA Config/FLASH.CLK
- U1 pad E10: unconnected-(U1-PadE10) -> /FPGA Config/JTAG.TCK
- U1 pad F10: unconnected-(U1-PadF10) -> /FPGA Config/JTAG.TMS
- U1 pad G10: unconnected-(U1-PadG10) -> /FPGA Config/JTAG.TDO
- U1 pad H10: unconnected-(U1-PadH10) -> /FPGA Config/JTAG.TDI
- U1 pad K10: unconnected-(U1-PadK10) -> /FPGA Config/PROGRAM_B
- U1 pad M10: unconnected-(U1-PadM10) -> /FPGA Config/DONE
- U1 pad P24: unconnected-(U1-PadP24) -> /FPGA banks 12-15/FLASH.DQ0
- U1 pad R20: unconnected-(U1-PadR20) -> /FPGA banks 12-15/FLASH.DQ2
- U1 pad R21: unconnected-(U1-PadR21) -> /FPGA banks 12-15/FLASH.DQ3
- U1 pad R25: unconnected-(U1-PadR25) -> /FPGA banks 12-15/FLASH.DQ1
- U1 pad T9: unconnected-(U1-PadT9) -> VCCO_0
- U1 pad U19: unconnected-(U1-PadU19) -> /FPGA banks 12-15/FLASH.~{CS}
- U3 pad 1: unconnected-(U3-Pad1) -> /FPGA Config/JTAG.TMS
- U3 pad 10: Net-(U3-Pad10) -> /FPGA Config/JTAG.TMS
- U3 pad 2: Net-(U3-Pad2) -> /FPGA Config/JTAG.TCK
- U3 pad 3: Net-(U3-Pad2) -> GND
- U3 pad 4: Net-(U3-Pad4) -> /FPGA Config/JTAG.TDO
- U3 pad 5: Net-(U3-Pad4) -> /FPGA Config/JTAG.TDI
- U3 pad 6: unconnected-(U3-Pad6) -> /FPGA Config/JTAG.TDI
- U3 pad 7: unconnected-(U3-Pad7) -> /FPGA Config/JTAG.TDO
- U3 pad 8: Net-(U3-Pad8) -> GND
- U3 pad 9: Net-(U3-Pad8) -> /FPGA Config/JTAG.TCK
- U4 pad 1: unconnected-(U4-Pad1) -> Net-(C61-Pad1)
- U4 pad 10: unconnected-(U4-Pad10) -> GND
- U4 pad 13: unconnected-(U4-Pad13) -> GND
- U4 pad 14: unconnected-(U4-Pad14) -> VOUT1
- U4 pad 15: unconnected-(U4-Pad15) -> VOUT1
- U4 pad 16: unconnected-(U4-Pad16) -> GND
- U4 pad 17: unconnected-(U4-Pad17) -> GND
- U4 pad 18: unconnected-(U4-Pad18) -> VOUT1
- U4 pad 2: unconnected-(U4-Pad2) -> GND
- U4 pad 20: unconnected-(U4-Pad20) -> GND
- U4 pad 22: unconnected-(U4-Pad22) -> VOUT4
- U4 pad 23: GND -> VOUT4
- U4 pad 24: VIN -> VOUT4
- U4 pad 25: VIN -> Net-(C56-Pad1)
- U4 pad 26: Net-(C59-Pad1) -> unconnected-(U4-Pad26)
- U4 pad 27: Net-(C59-Pad1) -> GND
- U4 pad 28: Net-(C59-Pad2) -> VIN
- U4 pad 29: Net-(Q1-Pad5) -> VIN
- U4 pad 30: unconnected-(U4-Pad30) -> Net-(C61-Pad1)
- U4 pad 31: Net-(Q1-Pad2) -> unconnected-(U4-Pad31)
- U4 pad 32: Net-(C58-Pad2) -> Net-(C61-Pad1)
- U4 pad 33: Net-(C58-Pad1) -> GND
- U4 pad 4: VIN -> unconnected-(U4-Pad4)
- U4 pad 5: unconnected-(U4-Pad5) -> GND
- U4 pad 6: unconnected-(U4-Pad6) -> VOUT2
- U4 pad 7: unconnected-(U4-Pad7) -> GND
- U4 pad 8: VIN -> VOUT2
- U4 pad 9: VIN -> VOUT2
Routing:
- net VCCO_0: track 0.00 -> 1.41 mm, vias 0 -> 2
- net unconnected-(U1-PadU19): track 0.71 -> 0.00 mm, vias 1 -> 0
- net unconnected-(U1-PadT9): track 0.71 -> 0.00 mm, vias 1 -> 0
- net unconnected-(U1-PadR25): track 0.71 -> 0.00 mm, vias 1 -> 0
- net unconnected-(U1-PadR21): track 0.71 -> 0.00 mm, vias 1 -> 0
- net unconnected-(U1-PadR20): track 0.71 -> 0.00 mm, vias 1 -> 0
- net unconnected-(U1-PadP24): track 0.71 -> 0.00 mm, vias 1 -> 0
- net unconnected-(U1-PadM10): track 0.71 -> 0.00 mm, vias 1 -> 0
- net unconnected-(U1-PadK10): track 0.71 -> 0.00 mm, vias 1 -> 0
- net unconnected-(U1-PadH10): track 0.71 -> 0.00 mm, vias 1 -> 0
- net unconnected-(U1-PadG10): track 0.71 -> 0.00 mm, vias 1 -> 0
- net unconnected-(U1-PadF10): track 0.71 -> 0.00 mm, vias 1 -> 0
- net unconnected-(U1-PadE10): track 0.71 -> 0.00 mm, vias 1 -> 0
- net unconnected-(U1-PadB10): track 0.71 -> 0.00 mm, vias 1 -> 0
- net unconnected-(U1-PadAB6): track 0.71 -> 0.00 mm, vias 1 -> 0
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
